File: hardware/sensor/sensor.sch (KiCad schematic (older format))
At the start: 71 parts, among them J1 Conn_01x02_Female, J2 Conn_01x06_Female, J3 Conn_01x03_Male, Q1 Q_PMOS_DGS, Q2 Q_NMOS_DGS, U1 L5973D, U2 L5973D, U3 ATSAMD21G18A-A, U4 BME280, U5 AT24CS04-STUM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

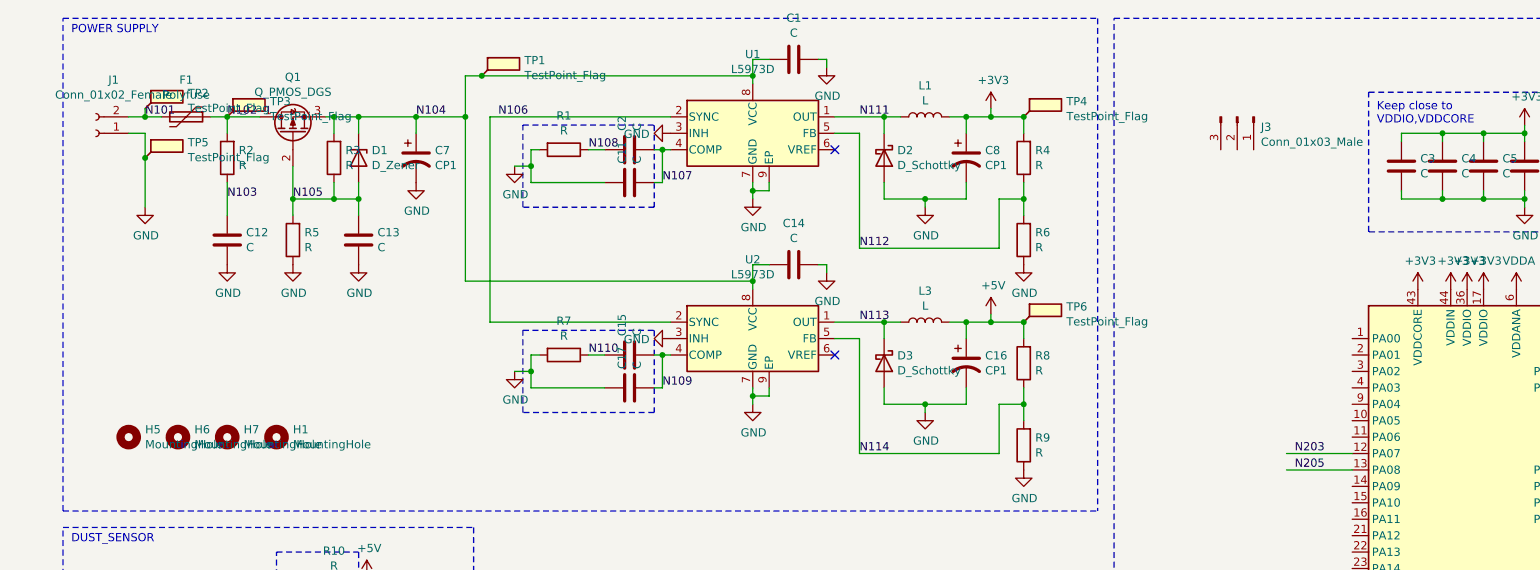
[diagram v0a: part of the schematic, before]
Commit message: Initial layout is complete
Removes mounting points as they're present in the DXF
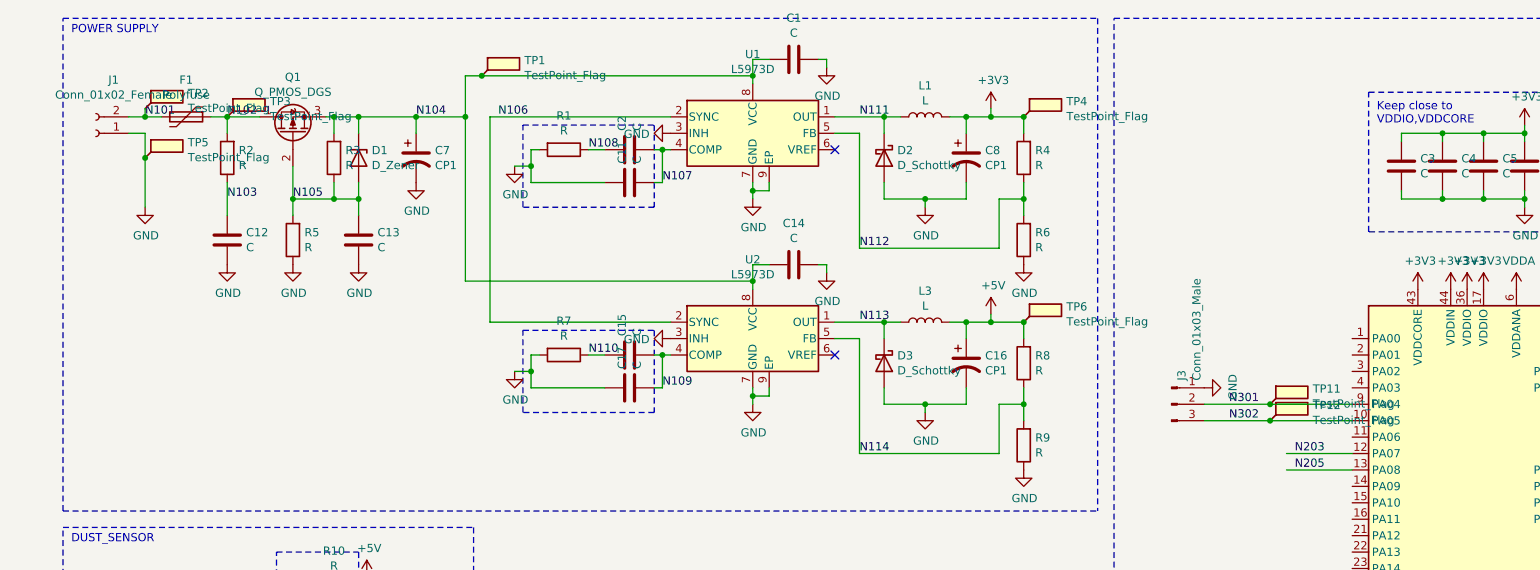
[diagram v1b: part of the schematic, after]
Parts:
- removed H1, H5, H6, H7: MountingHole, MountingHole:MountingHole_3mm, symbol Mechanical:MountingHole
- added TP11, TP12: TestPoint_Flag, TestPoint:TestPoint_Pad_D1.5mm, symbol Connector:TestPoint_Flag
- J3: footprint (none) -> Connector_PinHeader_2.54mm:PinHeader_1x03_P2.54mm_Vertical
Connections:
- net GND: now also J3.1 (Pin_1)
- net N302: now reaches U3.10 (PA05)
- net N302: now also J3.3 (Pin_3), TP12.1
- net N301: now reaches U3.9 (PA04)
- net N301: now also J3.2 (Pin_2), TP11.1
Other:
- moved on the sheet: J3
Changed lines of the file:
@@
-	1    0    0    -1
-$EndComp
-$Comp
-L Mechanical:MountingHole H5
-U 1 1 6052CF12
-P 1150 3200
-F 0 "H5" H 1250 3246 50  0000 L CNN
-F 1 "MountingHole" H 1250 3155 50  0000 L CNN
-F 2 "MountingHole:MountingHole_3mm" H 1150 3200 50  0001 C CNN
-F 3 "~" H 1150 3200 50  0001 C CNN
-	1    1150 3200
-	1    0    0    -1
-$EndComp
-$Comp
-L Mechanical:MountingHole H6
-U 1 1 605478EB
-P 1450 3200
-F 0 "H6" H 1550 3246 50  0000 L CNN
-F 1 "MountingHole" H 1550 3155 50  0000 L CNN
-F 2 "MountingHole:MountingHole_3mm" H 1450 3200 50  0001 C CNN
-F 3 "~" H 1450 3200 50  0001 C CNN
-	1    1450 3200
-	1    0    0    -1
-$EndComp
-$Comp
-L Mechanical:MountingHole H7
-U 1 1 60547B12
-P 1750 3200
-F 0 "H7" H 1850 3246 50  0000 L CNN
-F 1 "MountingHole" H 1850 3155 50  0000 L CNN
-F 2 "MountingHole:MountingHole_3mm" H 1750 3200 50  0001 C CNN
-F 3 "~" H 1750 3200 50  0001 C CNN
-	1    1750 3200
 	1    0    0    -1
 $EndComp
@@
 Text Label 8250 3300 0    50   ~ 0
 N203
-$Comp
-L Mechanical:MountingHole H1
-U 1 1 60664E2F
-P 2050 3200
-F 0 "H1" H 2150 3246 50  0000 L CNN
-F 1 "MountingHole" H 2150 3155 50  0000 L CNN
-F 2 "MountingHole:MountingHole_3mm" H 2050 3200 50  0001 C CNN
-F 3 "~" H 2050 3200 50  0001 C CNN
-	1    2050 3200
-	1    0    0    -1
-$EndComp
 $Comp
 L Connector:TestPoint_Flag TP9
@@
 Wire Wire Line
 	6300 6900 6100 6900
-Wire Bus Line
-	4400 5950 4400 6550
-Wire Bus Line
-	3100 5950 3100 6650
-Wire Bus Line
-	2000 5950 2000 6550
-Wire Bus Line
-	10550 3500 10550 6250
-Wire Bus Line
-	6400 5950 6400 6800
 Text Label 6250 6700 0    50   ~ 0
 I2C_SCL
@@
 L Connector:Conn_01x03_Male J3
 U 1 1 606F26C9
-P 7900 1250
-F 0 "J3" V 7962 1394 50  0000 L CNN
-F 1 "Conn_01x03_Male" V 8053 1394 50  0000 L CNN
-F 2 "" H 7900 1250 50  0001 C CNN
-F 3 "~" H 7900 1250 50  0001 C CNN
-	1    7900 1250
-	0    1    1    0
+P 7500 3000
+F 0 "J3" V 7562 3144 50  0000 L CNN
+F 1 "Conn_01x03_Male" V 7653 3144 50  0000 L CNN
+F 2 "Connector_PinHeader_2.54mm:PinHeader_1x03_P2.54mm_Vertical" H 7500 3000 50  0001 C CNN
+F 3 "~" H 7500 3000 50  0001 C CNN
+	1    7500 3000
+	1    0    0    -1
 $EndComp
+$Comp
+L power:GND #PWR0113
+U 1 1 60532836
+P 7700 2900
+F 0 "#PWR0113" H 7700 2650 50  0001 C CNN
+F 1 "GND" H 7705 2727 50  0000 C CNN
+F 2 "" H 7700 2900 50  0001 C CNN
+F 3 "" H 7700 2900 50  0001 C CNN
+	1    7700 2900
+	0    -1   -1   0
+$EndComp
+Wire Wire Line
+	7700 3100 8100 3100
+Wire Wire Line
+	7700 3000 8100 3000
+Text Label 7850 3000 0    50   ~ 0
+N301
+Text Label 7850 3100 0    50   ~ 0
+N302
+$Comp
+L Connector:TestPoint_Flag TP11
+U 1 1 605799C6
+P 8100 3000
+F 0 "TP11" H 8360 3094 50  0000 L CNN
+F 1 "TestPoint_Flag" H 8360 3003 50  0000 L CNN
+F 2 "TestPoint:TestPoint_Pad_D1.5mm" H 8300 3000 50  0001 C CNN
+F 3 "~" H 8300 3000 50  0001 C CNN
+	1    8100 3000
+	1    0    0    -1
+$EndComp
+Connection ~ 8100 3000
+Wire Wire Line
+	8100 3000 8600 3000
+$Comp
+L Connector:TestPoint_Flag TP12
+U 1 1 60579F95
+P 8100 3100
+F 0 "TP12" H 8360 3194 50  0000 L CNN
+F 1 "TestPoint_Flag" H 8360 3103 50  0000 L CNN
+F 2 "TestPoint:TestPoint_Pad_D1.5mm" H 8300 3100 50  0001 C CNN
+F 3 "~" H 8300 3100 50  0001 C CNN
+	1    8100 3100
+	1    0    0    -1
+$EndComp
+Connection ~ 8100 3100
+Wire Wire Line
+	8100 3100 8600 3100
+Wire Bus Line
+	4400 5950 4400 6550
+Wire Bus Line
+	3100 5950 3100 6650
+Wire Bus Line
+	2000 5950 2000 6550
+Wire Bus Line
+	10550 3500 10550 6250
+Wire Bus Line
+	6400 5950 6400 6800
 $EndSCHEMATC
